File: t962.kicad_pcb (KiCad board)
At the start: 2 copper layers, 40 x 45 mm, 40 parts, among them J1 Conn_01x03, J10 Conn_01x04, J2 TE 282834-8, J3 Conn_01x02_Male, J4 Conn_01x02_Male, J5 Conn_01x02_Male, J7 2.54mm pin header, J8 USB_B_Micro, Q1 BSS214NW, SW1 SW_SPST_KMR2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

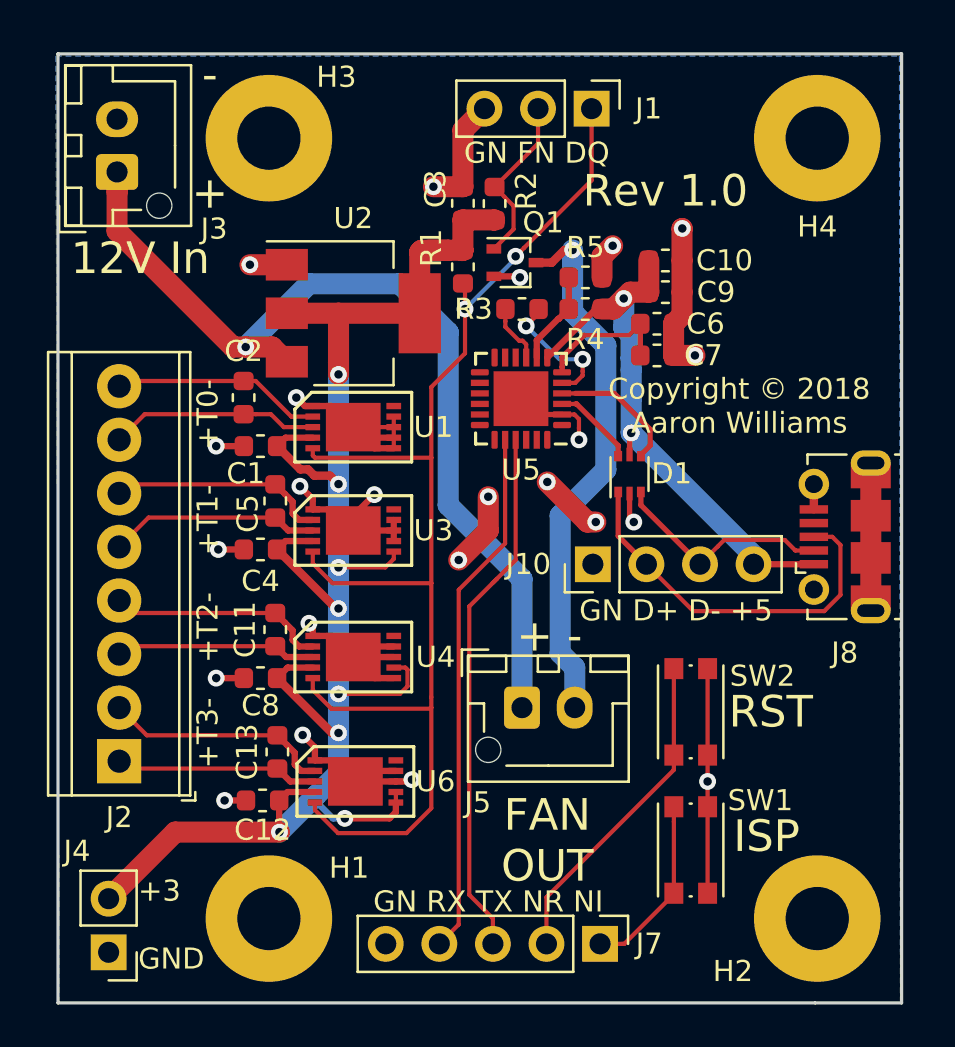
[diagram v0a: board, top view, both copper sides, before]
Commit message: Fixed 12V connectors and USB to serial
This swaps +12 and GND on the 12V and fan connectors and adds a second
12v connector for bypassing the fan control if desired.  Additionally,
the SI2102N is now powered from the 3.3V supply instead of the USB bus.

Updated to revision 1.1.

Signed-off-by: Aaron Williams <aaron.w2@gmail.com>
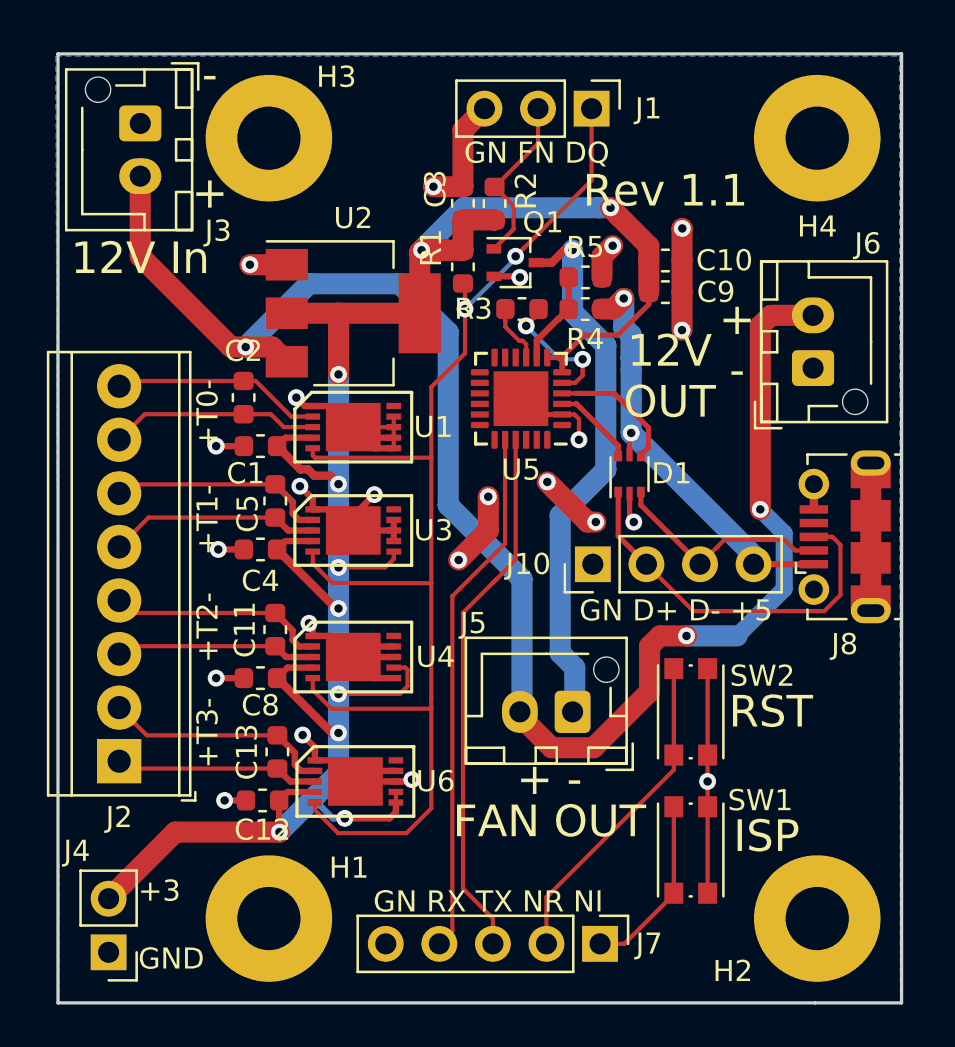
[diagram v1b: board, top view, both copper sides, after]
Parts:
- removed C6: 4.7uF, Capacitor_SMD:C_0603_1608Metric
- removed C7: 0.1uF, Capacitor_SMD:C_0603_1608Metric
- added J6: Conn_01x02_Male, Connector_JST:JST_XH_B02B-XH-AM_1x02_P2.50mm_Vertical, F.Cu at (163.7, 46.0)
- moved J3 2.55 mm to (131.8, 34.4), turned to 270 degrees
- moved J5 2.41 mm to (152.3, 62.3), turned to 180 degrees
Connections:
- C10 pad 1: +5V -> +3V3
- C9 pad 1: +5V -> +3V3
- J3 pad 1: +12V -> GND
- J3 pad 2: GND -> +12V
- J5 pad 1: +12V -> /FAN_PWM_OUT
- J5 pad 2: /FAN_PWM_OUT -> +12V
- U5 pad 6: Net-(C6-Pad1) -> +3V3
- U5 pad 7: +5V -> +3V3
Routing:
- net +12V: track 44.6 -> 77.5 mm, vias 1 -> 3
- net +3V3: track 85.1 -> 106.8 mm, vias 8 -> 10
- net Net-(C6-Pad1): track 6.58 -> 0.00 mm
- net +5V: track 26.7 -> 20.6 mm
- net GND: track 94.7 -> 92.4 mm
- added copper zone on F.Cu, net GND
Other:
- board text added: "12V OUT"
- board text added: "Rev 1.1"
- board text removed: "Rev 1.0"

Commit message: Updated BOM
Signed-off-by: Aaron Williams <aaron.w2@gmail.com>
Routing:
- net GND: track 92.4 -> 80.5 mm, vias 23 -> 34
- net +3V3: track 106.8 -> 103.0 mm
- net /FAN_PWM: track 8.26 -> 10.4 mm
- net /DQ: track 63.5 -> 63.1 mm, vias 2 -> 0
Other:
- board text added: "J3: 12V in J5: Fan out J6: 12V out"
- board text removed: "J3: 12V in J5: Fan out"

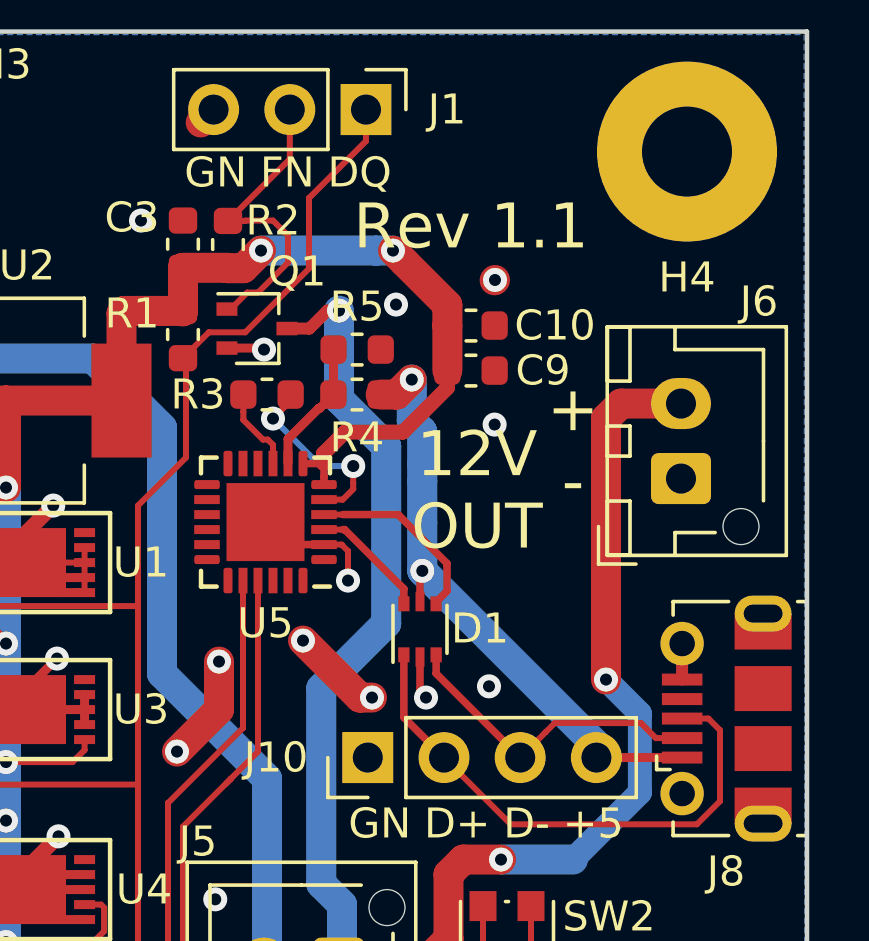
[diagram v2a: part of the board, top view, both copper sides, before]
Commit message: This fixes the VIO input so it is properly powered. Additionally, the footprint for the USBLC6-2SC6 has been fixed to a SOT23-6 which is a bigger footprint than the SOT666 that was there.
Signed-off-by: Aaron Williams <aaron.w2@gmail.com>
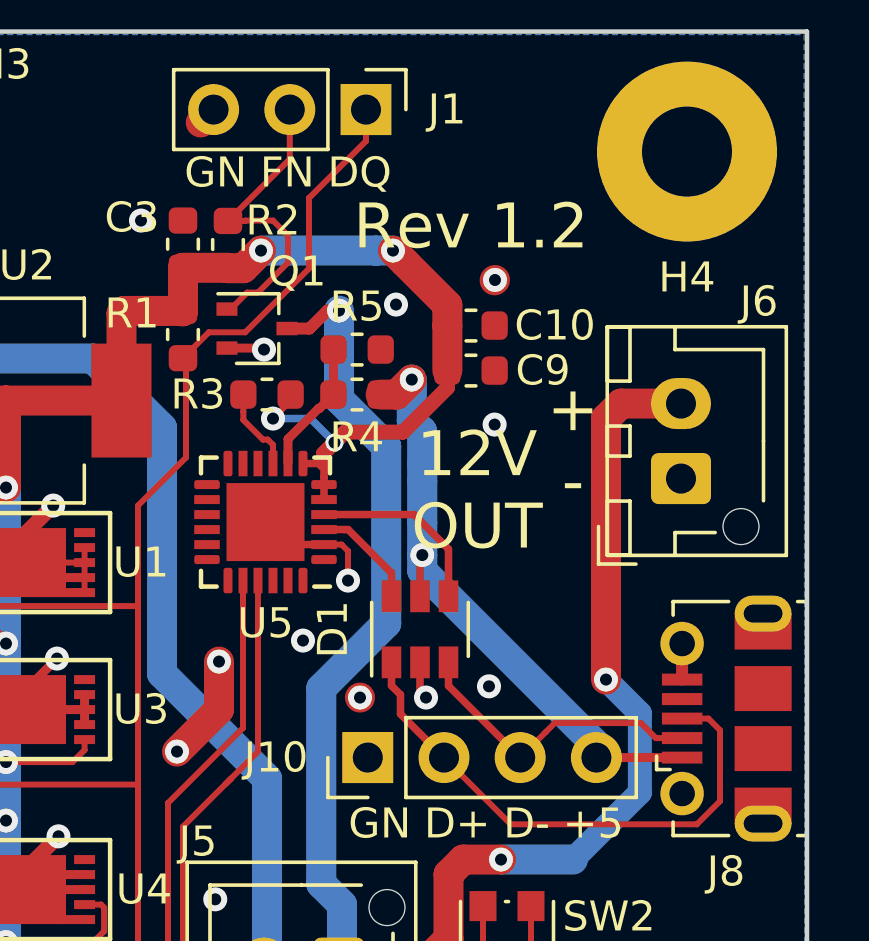
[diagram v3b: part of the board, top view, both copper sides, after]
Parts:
- D1: footprint Package_TO_SOT_SMD:SOT-666 -> Package_TO_SOT_SMD:SOT-23-6
- J3, J5, J6: value Conn_01x02_Male -> JST XH-B02B-XH-AM
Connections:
- R3 pad 1: /VIO -> +3V3
- U5 pad 5: /VIO -> +3V3
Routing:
- net /VIO: track 6.26 -> 0.00 mm, vias 2 -> 0
- net +3V3: track 103.0 -> 106.9 mm, vias 10 -> 12
- net GND: track 80.5 -> 77.4 mm
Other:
- board text added: "Rev 1.2"
- board text removed: "Rev 1.1"

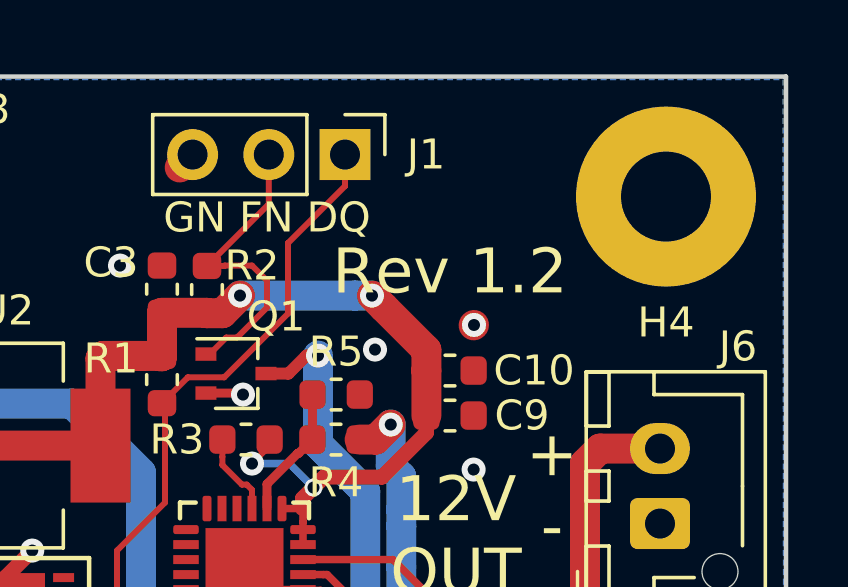
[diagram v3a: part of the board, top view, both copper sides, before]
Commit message: Fixed solder mask clearance.
Signed-off-by: Aaron Williams <aaron.w2@gmail.com>
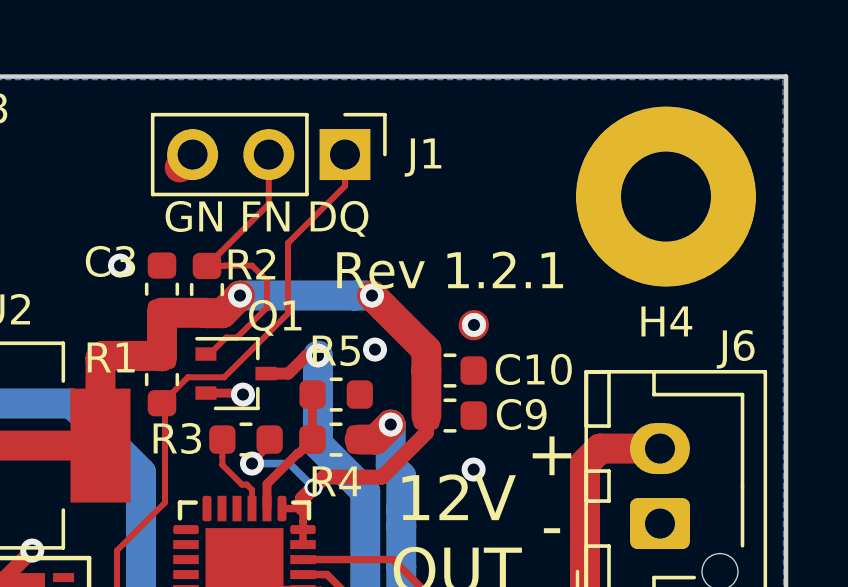
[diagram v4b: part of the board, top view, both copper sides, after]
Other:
- rule pad_to_mask_clearance: 0.051 -> -0.0504
- board text added: "Rev 1.2.1"
- board text removed: "Rev 1.2"
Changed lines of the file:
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@@
   (title_block
     (title "T-962 Temp Monitor and Fan Controller")
-    (date 2019-01-05)
-    (rev 1.2)
+    (date 2019-01-25)
+    (rev 1.2.1)
     (company "Copyright © 2018 by Aaron Williams")
   )
@@
     (pad_size 1.524 1.524)
     (pad_drill 0.762)
-    (pad_to_mask_clearance 0.051)
+    (pad_to_mask_clearance -0.0504)
     (solder_mask_min_width 0.25)
     (aux_axis_origin 0 0)
@@
     (effects (font (size 1.5 1.5) (thickness 0.3)))
   )
-  (gr_text "Rev 1.2" (at 156.7 37.6) (layer F.SilkS)
-    (effects (font (size 1.5 1.5) (thickness 0.3)))
+  (gr_text "Rev 1.2.1" (at 156.7 37.6) (layer F.SilkS)
+    (effects (font (size 1.2 1.2) (thickness 0.25)))
   )
   (gr_text "Copyright © 2018\nAaron Williams" (at 160.6 62.7) (layer B.SilkS)

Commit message: Fixed solder mask again and included pictures.
Signed-off-by: Aaron Williams <aaron.w2@gmail.com>
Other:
- rule pad_to_mask_clearance: -0.0504 -> 0.0504
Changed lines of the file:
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@@
     (pad_size 1.524 1.524)
     (pad_drill 0.762)
-    (pad_to_mask_clearance -0.0504)
+    (pad_to_mask_clearance 0.0504)
     (solder_mask_min_width 0.25)
     (aux_axis_origin 0 0)

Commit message: Fixed pad mask clearance.
Signed-off-by: aaronw <aaron.w2@gmail.com>
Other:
- rule solder_mask_min_width: 0.25 -> 0.1
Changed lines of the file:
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@@
   (title_block
     (title "T-962 Temp Monitor and Fan Controller")
-    (date 2019-01-25)
-    (rev 1.2.1)
+    (date 2019-02-08)
+    (rev 1.2.2)
     (company "Copyright © 2018 by Aaron Williams")
   )
@@
     (pad_drill 0.762)
     (pad_to_mask_clearance 0.0504)
-    (solder_mask_min_width 0.25)
+    (solder_mask_min_width 0.1)
     (aux_axis_origin 0 0)
     (visible_elements FFFFFF7F)

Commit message: Fixed solder mask min width again.
Signed-off-by: aaronw <aaron.w2@gmail.com>
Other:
- rule solder_mask_min_width: 0.1 -> 0.25
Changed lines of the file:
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@@
     (pad_drill 0.762)
     (pad_to_mask_clearance 0.0504)
-    (solder_mask_min_width 0.1)
+    (solder_mask_min_width 0.25)
     (aux_axis_origin 0 0)
     (visible_elements FFFFFF7F)

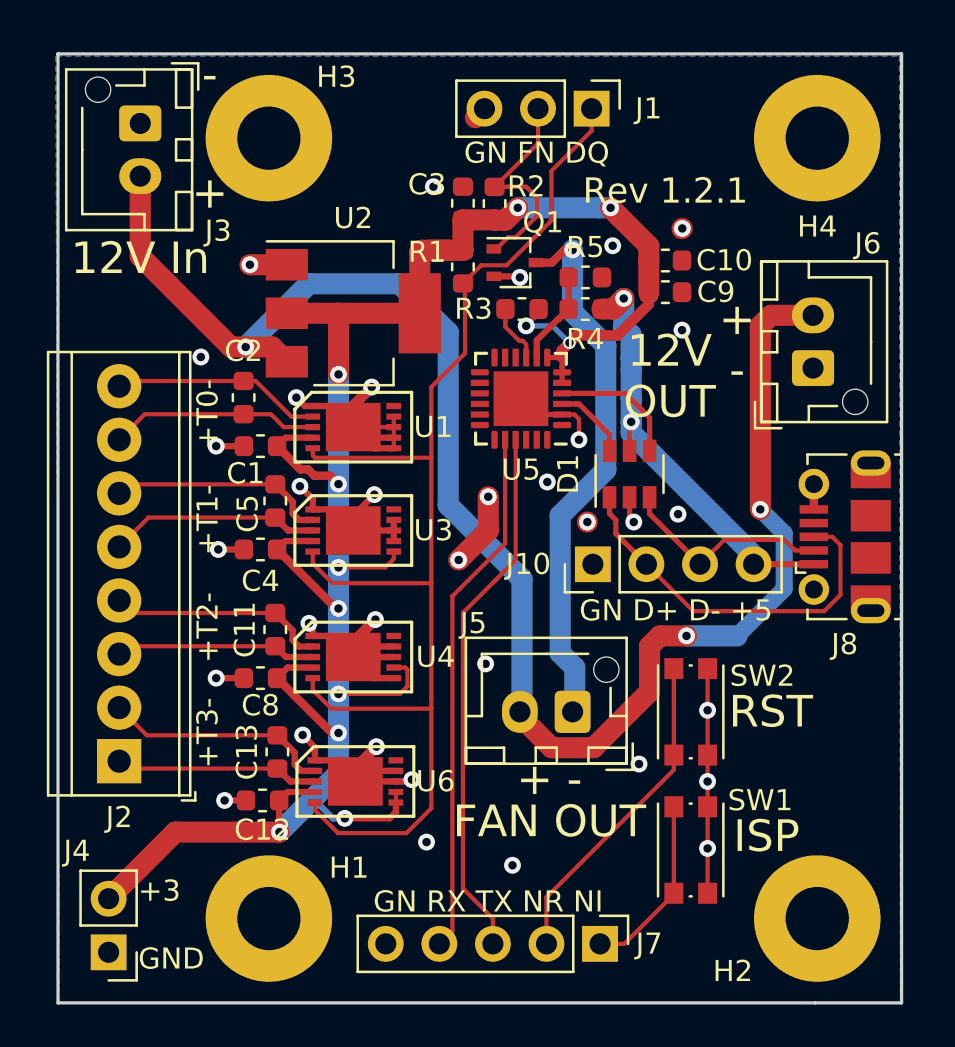
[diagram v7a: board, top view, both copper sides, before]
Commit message: Swap TX/RX and add connector to expose RST and NI
TX and RX were swapped from what they should be.  This
fixes that.  Additionally, J9 was added so that external
buttons can be added for NI and RST.

Signed-off-by: aaronw <aaron.w2@gmail.com>
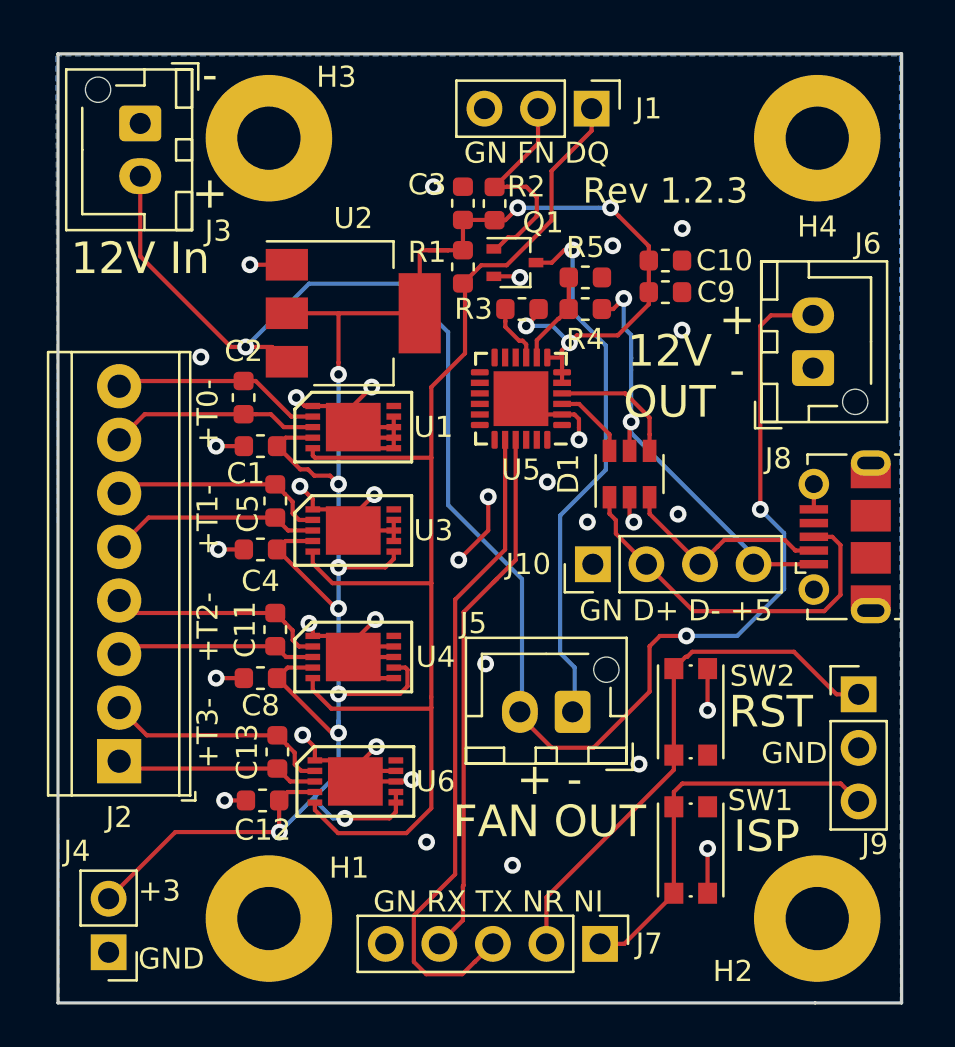
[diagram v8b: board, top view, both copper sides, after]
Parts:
- added J9: Conn_01x03_Male, Connector_PinHeader_2.54mm:PinHeader_1x03_P2.54mm_Vertical, F.Cu at (165.9, 61.5)
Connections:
- U5 pad 20: /RXD0 -> /TXD0
- U5 pad 21: /TXD0 -> /RXD0
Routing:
- net /N_ISP: track 8.62 -> 18.6 mm
- net /N_RST: track 15.6 -> 25.5 mm
- net GND: track 77.4 -> 70.8 mm, vias 34 -> 33
- net /TXD0: track 25.8 -> 31.1 mm
- net /RXD0: track 25.2 -> 25.8 mm
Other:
- rule solder_mask_min_width: 0.25 -> 0.1
- board text added: "GND"
- board text added: "Rev 1.2.3"
- board text removed: "Rev 1.2.1"
